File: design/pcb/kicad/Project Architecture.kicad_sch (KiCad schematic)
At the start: 0 parts

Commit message: Add LCD and STLink schematic sheets, update KiCad project files
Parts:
- added BOOT0: SW3, Button_Switch_SMD:SW_Tactile_SPST_NO_Straight_CK_PTS636Sx25SMTRLFS, symbol Switch:SW_Push
- added C1, C15, C18, C2, C20, C21, C3: 100nF, Capacitor_SMD:C_0402_1005Metric, symbol Device:C
- added C10, C17, C7, C8: 1uF, Capacitor_SMD:C_0402_1005Metric, symbol Device:C
- added C19: 2.2nF, Capacitor_SMD:C_0402_1005Metric, symbol Device:C
- added C4: 4.7uF, Capacitor_SMD:C_0402_1005Metric, symbol Device:C
- added C5, C6: 20pF, Capacitor_SMD:C_0402_1005Metric, symbol Device:C
- added C9: 10nF, Capacitor_SMD:C_0402_1005Metric, symbol Device:C
- added D1, D4, D8: RED LED, LED_SMD:LED_0603_1608Metric, symbol Device:LED
- added D2: BLUE LED, LED_SMD:LED_0603_1608Metric, symbol Device:LED
- added D3: GREEN LED, LED_SMD:LED_0603_1608Metric, symbol Device:LED
- added D6: 1N5819WS, Diode_SMD:D_SOD-323, symbol Diode:1N5819WS
- added H1, H2, H3, H4: MountingHole, MountingHole:MountingHole_2.2mm_M2, symbol Mechanical:MountingHole
- added J2: USB_B_Micro, FB_Library:micro_USB, symbol Connector:USB_B_Micro
- added P1, P2, P3: Conn_02x05_Odd_Even, Connector_PinSocket_2.54mm:PinSocket_2x05_P2.54mm_Vertical_SMD, symbol Connector_Generic:Conn_02x05_Odd_Even
- added R1, R14, R15, R16, R2, R24, R9: 330, Resistor_SMD:R_0402_1005Metric, symbol Device:R
- added R10, R11: 2.2K, Resistor_SMD:R_0402_1005Metric, symbol Device:R
- added R12, R3: 100, Resistor_SMD:R_0402_1005Metric, symbol Device:R
- added R13, R19, R4, R8: 10K, Resistor_SMD:R_0402_1005Metric, symbol Device:R
- added R5, R6: 20, Resistor_SMD:R_0402_1005Metric, symbol Device:R
- added R7: 1.5K, Resistor_SMD:R_0402_1005Metric, symbol Device:R
- added RESET1: SW1, Button_Switch_SMD:SW_Tactile_SPST_NO_Straight_CK_PTS636Sx25SMTRLFS, symbol Switch:SW_Push
- added U1: STM32F303CCTx, Package_QFP:LQFP-48_7x7mm_P0.5mm, symbol MCU_ST_STM32F3:STM32F303CCTx
- added U4: CDSOT236-0504C, Package_TO_SOT_SMD:SOT-23-6, symbol Power_Protection:CDSOT236-0504C
- added U5: TLV75733PDBV, Package_TO_SOT_SMD:SOT-23-5, symbol Regulator_Linear:TLV75733PDBV
- added U8: MPU6050, Package_DFN_QFN:QFN-24-1EP_4x4mm_P0.5mm_EP2.7x2.6mm, symbol MPU:MPU6050
- added USER1: SW2, Button_Switch_SMD:SW_Tactile_SPST_NO_Straight_CK_PTS636Sx25SMTRLFS, symbol Switch:SW_Push
- added Y1: 8MHz Crystal, Crystal:Crystal_SMD_HC49-SD, symbol Device:Crystal
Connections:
- new net: D8.2 (A), R24.2
- new net: D4.2 (A), R16.2
- new net: R19.2, U1.20 (PB2)
- new net: J2.2 (D-), R6.1, U4.3 (IO2)
- new net: J2.3 (D+), R5.1, U4.1 (IO1)
- new net: D1.2 (A), R1.2
- new net: D2.2 (A), R2.2
- new net: BOOT0.1, C15.2, R8.2, R9.1
- new net: C20.1, U8.10 (REGOUT)
- new net: C19.1, U8.20 (CPOUT)
- new net: C21.2, R13.2, R14.1, USER1.1
- new net: C15.1, R3.2
- new net: C21.1, R12.2
- new net: D6.2 (A), J2.1 (VBUS), U4.5 (VP)
- new net: D3.2 (A), R15.2
- new net +3V3: BOOT0.2, C1.1, C17.1, C18.1, C2.1, C3.1, C4.1, C8.1, C9.1, P1.1 (Pin_1), P3.1 (Pin_1), R1.1, R10.1, R11.1, R12.1, R19.1, R3.1, R4.1, R7.1, U1.1 (VBAT), U1.24 (VDD), U1.36 (VDD), U1.48 (VDD), U1.9 (VDDA), U5.5 (OUT), U8.13 (VDD), U8.8 (VLOGIC), USER1.2
- new net +5V: C7.1, D6.1 (K), R24.1, U5.1 (IN), U5.3 (EN)
- new net BOOT0: R9.2, U1.44 (BOOT0)
- new net GND: C1.2, C10.2, C17.2, C18.2, C19.2, C2.2, C20.2, C3.2, C4.2, C5.1, C6.1, C7.2, C8.2, C9.2, D1.1 (K), D2.1 (K), D3.1 (K), D4.1 (K), D8.1 (K), J2.4 (ID), J2.5 (GND), J2.6 (Shield), P1.10 (Pin_10), P3.10 (Pin_10), R13.1, R8.1, RESET1.1, U1.23 (VSS), U1.35 (VSS), U1.47 (VSS), U1.8 (VSSA), U4.2 (VN), U5.2 (GND), U8.1 (CLKIN), U8.11 (FSYNC), U8.18 (GND), U8.25 (DP), U8.9 (AD0)
- new net I2C1_SCL: P3.6 (Pin_6), R10.2, U1.42 (PB6), U8.23 (SCL)
- new net I2C1_SDA: P3.7 (Pin_7), R11.2, U1.43 (PB7), U8.24 (SDA)
- new net LED_1: P1.3 (Pin_3), R2.1, U1.11 (PA1)
- new net LED_2: P1.4 (Pin_4), R15.1, U1.12 (PA2)
- new net LED_3: P1.5 (Pin_5), R16.1, U1.13 (PA3)
- new net MPU_INT: P3.2 (Pin_2), U1.29 (PA8), U8.12 (INT)
- new net OSC_IN: C5.2, U1.5 (PF0), Y1.2
- new net OSC_OUT: C6.2, U1.6 (PF1), Y1.1
- new net PA15: P3.3 (Pin_3), U1.38 (PA15)
- new net PA4: P1.6 (Pin_6), U1.14 (PA4)
- new net PA5: P1.7 (Pin_7), U1.15 (PA5)
- new net PA6: P1.8 (Pin_8), U1.16 (PA6)
- new net PA7: P1.9 (Pin_9), U1.17 (PA7)
- new net PB0: P2.1 (Pin_1), U1.18 (PB0)
- new net PB1: P2.2 (Pin_2), U1.19 (PB1)
- new net PB10: P2.3 (Pin_3), U1.21 (PB10)
- new net PB11: P2.4 (Pin_4), U1.22 (PB11)
- new net PB12: P2.5 (Pin_5), U1.25 (PB12)
- new net PB13: P2.6 (Pin_6), U1.26 (PB13)
- new net PB14: P2.7 (Pin_7), U1.27 (PB14)
- new net PB15: P2.8 (Pin_8), U1.28 (PB15)
- new net PB4: P3.4 (Pin_4), U1.40 (PB4)
- new net PB5: P3.5 (Pin_5), U1.41 (PB5)
- new net PB8: P3.8 (Pin_8), U1.45 (PB8)
- new net PB9: P3.9 (Pin_9), U1.46 (PB9)
- new net PC13: P1.2 (Pin_2), U1.2 (PC13)
- new net RESET: C10.1, R4.2, RESET1.2, U1.7 (NRST)
- new net SWCLK: U1.37 (PA14)
- new net SWDIO: U1.34 (PA13)
- new net SWO: U1.39 (PB3)
- new net USART1_RX: P2.10 (Pin_10), U1.31 (PA10)
- new net USART1_TX: P2.9 (Pin_9), U1.30 (PA9)
- new net USB_DM: R6.2, U1.33 (PA12)
- new net USB_DP: R5.2, R7.2, U1.32 (PA11)
- new net USER_BTN: R14.2, U1.10 (PA0)
- no-connect marks 0 -> 6
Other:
- removed sheet LDO
- added sheet LCD (LCD.kicad_sch)
- added sheet stlinkv3 (stlinkv3.kicad_sch)
- note added: "3V3"
- note added: "BOOT 0 DEFAULT - LOW - MAIN FLASH MEMORY PRESSED - HIGH - SYSTEM MEMORY"
- note added: "BOOT 1"
- note added: "BOOT MODES"
- note added: "BUTTONS"
- note added: "GND"
- note added: "HEADER PINS"
- note added: "LED's"
- note added: "MICRO USB"
- note added: "MPU6050"
- note added: "MPU6050_INTERUPT"
- note added: "Mounting Holes"
- note added: "OSCILLATORS"
- note added: "PA0"
- note added: "PA1"
- note added: "PA10"
- note added: "PA15"
- note added: "PA2"
- note added: "PA3"
- note added: "PA4"
- note added: "PA5"
- note added: "PA6"
- note added: "PA7"
- note added: "PA8"
- note added: "PA9"
- note added: "PB0"
- note added: "PB1"
- note added: "PB10"
- note added: "PB11"
- note added: "PB12"
- note added: "PB13"
- note added: "PB14"
- note added: "PB15"
- note added: "PB4"
- note added: "PB5"
- note added: "PB6"
- note added: "PB7"
- note added: "PB8"
- note added: "PB9"
- note added: "PC13"
- note added: "PF0"
- note added: "PF1"
- note added: "POWER ON/OFF LED"
- note added: "RESET"
- note added: "STM32F303CCT6 MCU"
- note added: "USER"
- note added: "VOLTAGE REGULATOR"

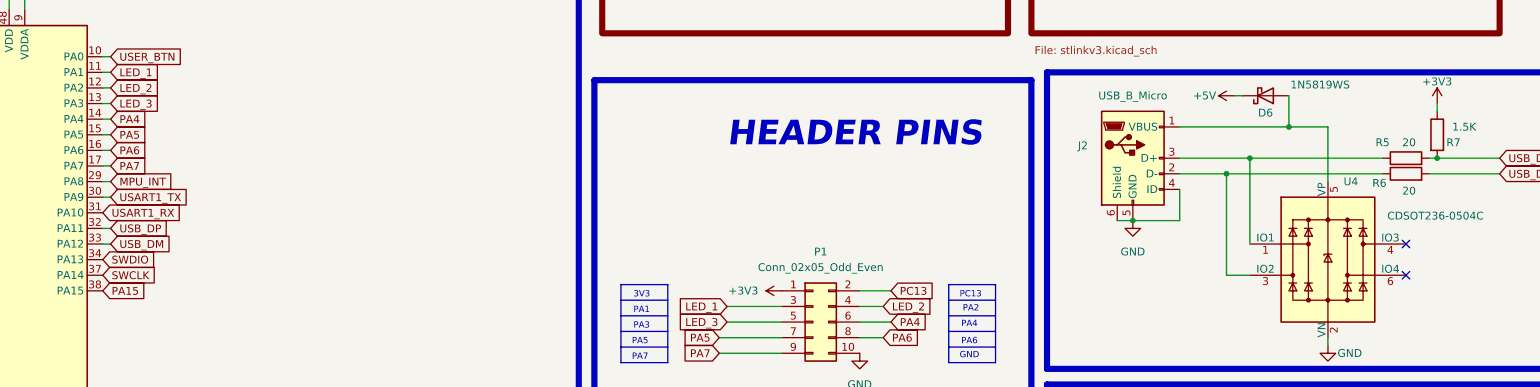
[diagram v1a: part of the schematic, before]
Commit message: Change of USB and STlink label
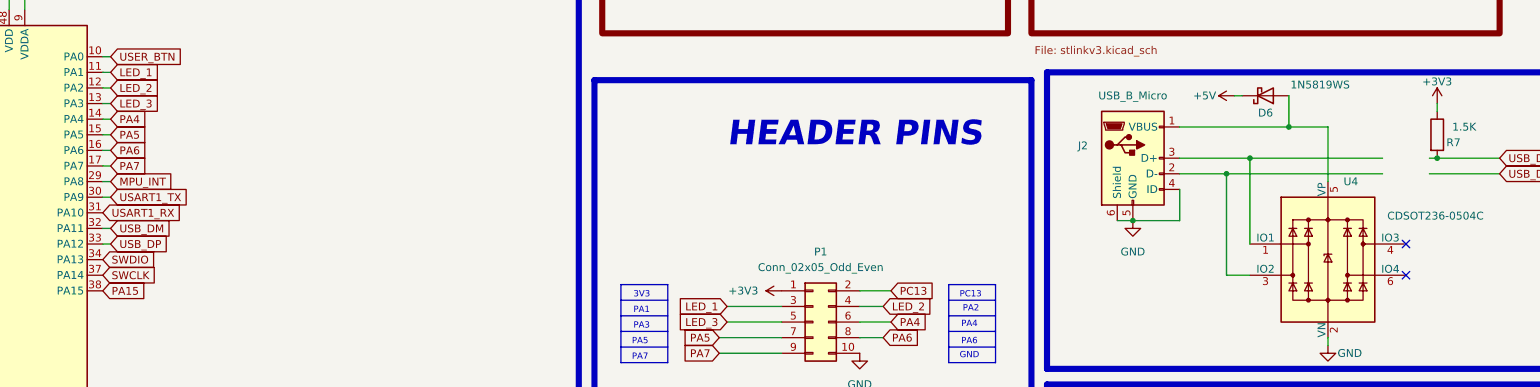
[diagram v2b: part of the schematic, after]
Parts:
- removed R5, R6: 20, Resistor_SMD:R_0402_1005Metric, symbol Device:R
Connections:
- net USB_DM: now also U1.32 (PA11); no longer U1.33 (PA12)
- net USB_DP: now also U1.33 (PA12); no longer U1.32 (PA11)

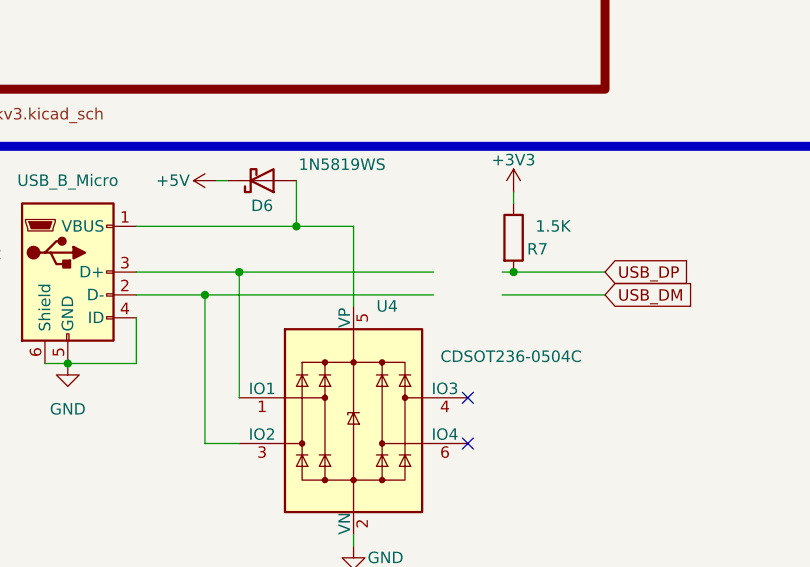
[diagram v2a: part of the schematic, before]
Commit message: Change of USB and STlink label
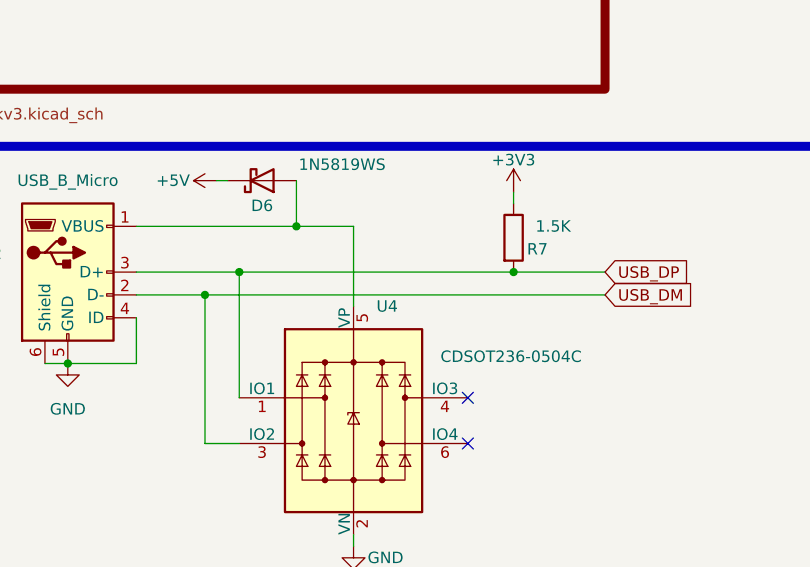
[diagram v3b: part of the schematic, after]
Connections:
- net USB_DM: now also J2.2 (D-), U4.3 (IO2)
- net USB_DP: now also J2.3 (D+), U4.1 (IO1)
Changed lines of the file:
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@@
 	(wire
 		(pts
-			(xy 293.37 81.28) (xy 318.77 81.28)
+			(xy 293.37 81.28) (xy 337.82 81.28)
 		)
 		(stroke
@@
 	(wire
 		(pts
-			(xy 326.39 78.74) (xy 327.66 78.74)
-		)
-		(stroke
-			(width 0)
-			(type default)
-		)
-	)
-	(wire
-		(pts
 			(xy 33.02 86.36) (xy 35.56 86.36)
 		)
@@
 	(wire
 		(pts
-			(xy 297.18 78.74) (xy 318.77 78.74)
+			(xy 297.18 78.74) (xy 327.66 78.74)
 		)
 		(stroke
@@
 		)
 		(stroke
-			(width 0)
-			(type default)
-		)
-	)
-	(wire
-		(pts
-			(xy 326.39 81.28) (xy 337.82 81.28)
-		)
-		(stroke

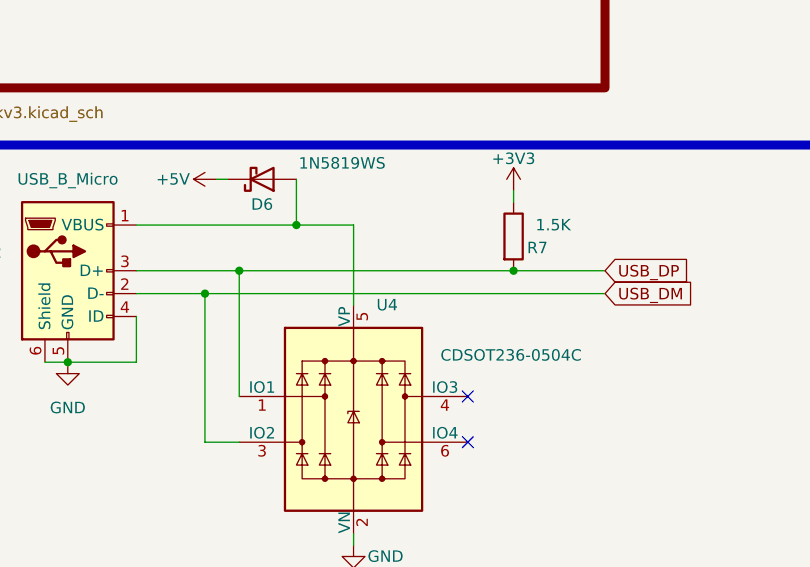
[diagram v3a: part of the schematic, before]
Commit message: Change of USB and STlink label
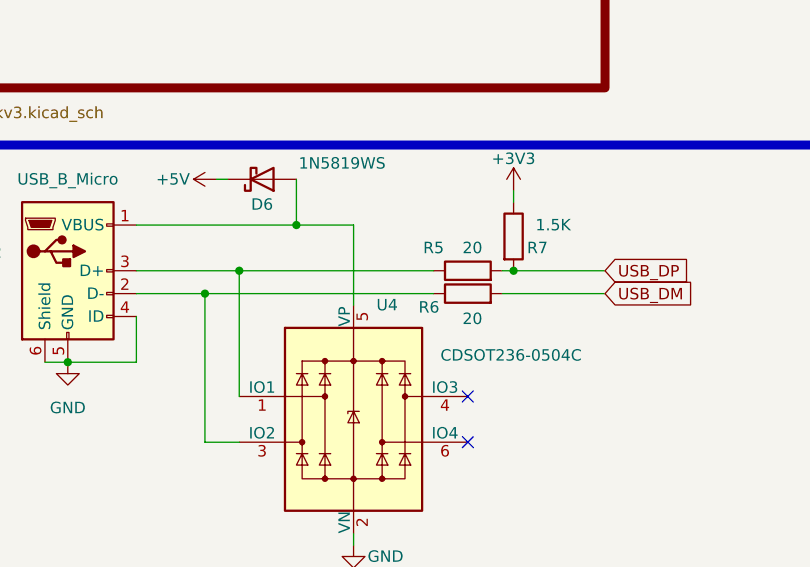
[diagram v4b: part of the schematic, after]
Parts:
- added R5, R6: 20, Resistor_SMD:R_0402_1005Metric, symbol Device:R
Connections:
- net USB_DM: now also R6.2; no longer J2.2 (D-), U4.3 (IO2)
- net USB_DP: now also R5.2; no longer J2.3 (D+), U4.1 (IO1)
- new net: J2.2 (D-), R6.1, U4.3 (IO2)
- new net: J2.3 (D+), R5.1, U4.1 (IO1)
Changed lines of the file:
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@@
 	(wire
 		(pts
-			(xy 293.37 81.28) (xy 337.82 81.28)
+			(xy 293.37 81.28) (xy 318.77 81.28)
 		)
 		(stroke
@@
 	(wire
 		(pts
+			(xy 326.39 78.74) (xy 327.66 78.74)
+		)
+		(stroke
+			(width 0)
+			(type default)
+		)
+	)
+	(wire
+		(pts
 			(xy 33.02 86.36) (xy 35.56 86.36)
 		)
@@
 	(wire
 		(pts
-			(xy 297.18 78.74) (xy 327.66 78.74)
+			(xy 297.18 78.74) (xy 318.77 78.74)
 		)
 		(stroke
@@
 		)
 	)
+	(wire
+		(pts
+			(xy 326.39 81.28) (xy 337.82 81.28)
+		)
+		(stroke
+			(width 0)
+			(type default)
+		)
+	)
 	(global_label "PA7"
 		(shape input)
@@
 	)
 	(symbol
+		(lib_id "Device:R")
+		(at 322.58 81.28 90)
+		(unit 1)
+		(exclude_from_sim no)
+		(in_bom yes)
+		(on_board yes)
+		(dnp no)
+		(property "Reference" "R6"
+			(at 318.262 82.804 90)
+			(effects
+				(font
+					(size 1.27 1.27)
+				)
+			)
+		)
+		(property "Value" "20"
+			(at 323.088 84.074 90)
+			(effects
+				(font
+					(size 1.27 1.27)
+				)
+			)
+		)
+		(property "Footprint" "Resistor_SMD:R_0402_1005Metric"
+			(at 322.58 83.058 90)
+			(effects
+				(font
+					(size 1.27 1.27)
+				)
+				(hide yes)
+			)
+		)
+		(property "Datasheet" "~"
+			(at 322.58 81.28 0)
+			(effects
+				(font
+					(size 1.27 1.27)
+				)
+				(hide yes)
+			)
+		)
+		(property "Description" "Resistor"
+			(at 322.58 81.28 0)
+			(effects
+				(font
+					(size 1.27 1.27)
+				)
+				(hide yes)
+			)
+		)
+		(property "MPN" "RC0402FR-0720RL "
+			(at 322.58 81.28 0)
+			(effects
+				(font
+					(size 1.27 1.27)
+				)
+				(hide yes)
+			)
+		)
+		(property "Manufacturer" "YAGEO "
+			(at 322.58 81.28 0)
+			(effects
+				(font
+					(size 1.27 1.27)
+				)
+				(hide yes)
+			)
+		)
+		(property "LCSC" "C138031"
+			(at 322.58 81.28 90)
+			(effects
+				(font
+					(size 1.27 1.27)
+				)
+				(hide yes)
+			)
+		)
+		(property "MANUFACTURER" "RC0402FR-0720RL"
+			(at 322.58 81.28 90)
+			(effects
+				(font
+					(size 1.27 1.27)
+				)
+				(hide yes)
+			)
+		)
+		(pin "1"
+		)
+		(pin "2"
+		)
+		(instances
+			(project "Swasthik_KiBot_Project"
+				(path "/f9e05184-c88b-4a88-ae9c-ab2bdb32be7c/c5103ceb-5325-4a84-a025-9638a412984e"
+					(reference "R6")
+					(unit 1)
+				)
+			)
+		)
+	)
+	(symbol
 		(lib_id "power:GND")
 		(at 360.68 181.61 90)
@@
 					(unit 1)
 				)
+			)
+		)
+	)
+	(symbol
+		(lib_id "Device:R")
+		(at 322.58 78.74 90)
+		(unit 1)
+		(exclude_from_sim no)
+		(in_bom yes)
+		(on_board yes)
+		(dnp no)
+		(property "Reference" "R5"
+			(at 318.77 76.2 90)
+			(effects
+				(font
+					(size 1.27 1.27)
+				)
+			)
+		)
+		(property "Value" "20"
+			(at 323.088 76.2 90)
+			(effects
+				(font
+					(size 1.27 1.27)
+				)
+			)
+		)
+		(property "Footprint" "Resistor_SMD:R_0402_1005Metric"
+			(at 322.58 80.01 90)
+			(effects
+				(font
+					(size 1.27 1.27)
+				)
+				(hide yes)
+			)
+		)
+		(property "Datasheet" "~"
+			(at 322.58 78.74 0)
+			(effects
+				(font
+					(size 1.27 1.27)
+				)
+				(hide yes)
+			)
+		)
+		(property "Description" "Resistor"
+			(at 322.58 78.74 0)
+			(effects
+				(font
+					(size 1.27 1.27)
+				)
+				(hide yes)
+			)
+		)
+		(property "MPN" "RC0402FR-0720RL "
+			(at 322.58 78.74 0)
+			(effects
+				(font
+					(size 1.27 1.27)
+				)
+				(hide yes)
+			)
+		)
+		(property "Manufacturer" "YAGEO "
+			(at 322.58 78.74 0)
+			(effects
+				(font
+					(size 1.27 1.27)
+				)
+				(hide yes)
+			)
+		)
+		(property "LCSC" "C138031"
+			(at 322.58 78.74 90)
+			(effects
+				(font
+					(size 1.27 1.27)
+				)
+				(hide yes)
+			)
+		)
+		(property "MANUFACTURER" "RC0402FR-0720RL"
+			(at 322.58 78.74 90)
+			(effects
+				(font
+					(size 1.27 1.27)
+				)
+				(hide yes)
+			)
+		)
+		(pin "1"
+		)
+		(pin "2"
+		)
+		(instances
+			(project "Swasthik_KiBot_Project"
+				(path "/f9e05184-c88b-4a88-ae9c-ab2bdb32be7c/c5103ceb-5325-4a84-a025-9638a412984e"
+					(reference "R5")
+					(unit 1)
+				)

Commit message: New Component
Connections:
- net USB_DM: no longer R6.2
- net USB_DP: no longer R5.2, R7.2
- new net: R5.2, R7.2
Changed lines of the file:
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@@
-	)
-	(junction
-		(at 327.66 78.74)
-		(diameter 0)
-		(color 0 0 0 0)
 	)
 	(junction
@@
 	(wire
 		(pts
-			(xy 327.66 78.74) (xy 337.82 78.74)
-		)
-		(stroke
-			(width 0)
-			(type default)
-		)
-	)
-	(wire
-		(pts
 			(xy 31.75 182.88) (xy 31.75 180.34)
 		)
@@
 		)
 		(stroke
-			(width 0)
-			(type default)
-		)
-	)
-	(wire
-		(pts
-			(xy 326.39 81.28) (xy 337.82 81.28)
-		)
-		(stroke
